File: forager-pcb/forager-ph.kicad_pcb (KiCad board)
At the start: 2 copper layers, 114.6 x 96.3 mm, 35 parts, among them J4 Conn_01x02_Pin

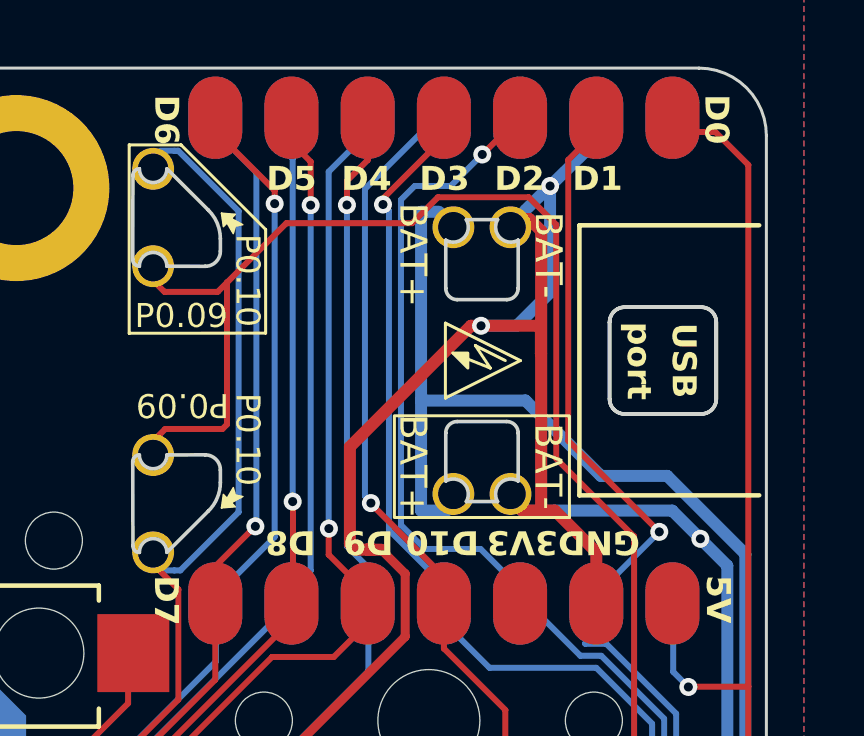
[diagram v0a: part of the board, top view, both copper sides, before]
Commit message: Re-inforce BAT+ connection with trace on both sides.
This may help if the copper is damaged while soldering, or when the
board is drilled during fabrication.
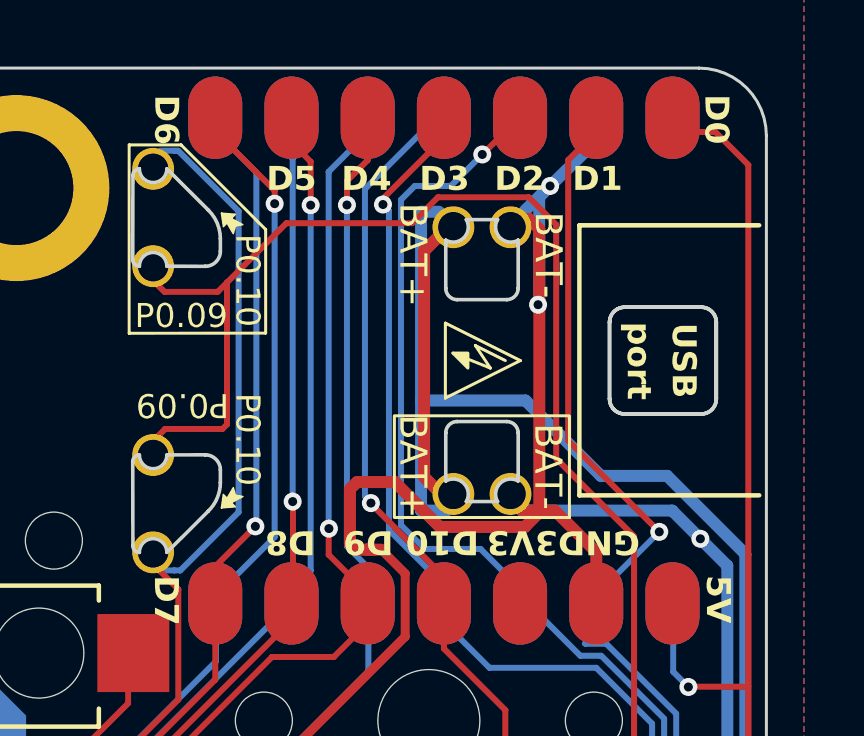
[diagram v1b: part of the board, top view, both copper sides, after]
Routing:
- net BAT: track 43.9 -> 52.9 mm
- net GND: track 204.8 -> 199.6 mm
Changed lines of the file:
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@@
 	)
 	(segment
-		(start 104.368 -37.128)
+		(start 104.561057 -33.697719)
 		(end 104.368 -33.890776)
 		(width 0.4)
@@
 	)
 	(segment
+		(start 110.639829 -41.862456)
+		(end 110.7135 -41.788785)
+		(width 0.4)
+		(layer "F.Cu")
+		(net 1)
+	)
+	(segment
 		(start 44.95 -19.83)
 		(end 44.95 -11.74)
@@
 	)
 	(segment
+		(start 110.68 -44.388023)
+		(end 110.353823 -44.7142)
+		(width 0.4)
+		(layer "F.Cu")
+		(net 1)
+	)
+	(segment
 		(start 101.575743 -0.325)
 		(end 105.19 -0.325)
@@
 	)
 	(segment
-		(start 108.74 -41.16)
-		(end 110.7135 -41.16)
+		(start 104.368 -35.71)
+		(end 104.609 -35.951)
 		(width 0.4)
 		(layer "F.Cu")
@@
 	)
 	(segment
-		(start 110.7335 -40.24)
-		(end 110.7435 -40.23)
+		(start 104.368 -33.890776)
+		(end 104.368 -35.71)
+		(width 0.4)
+		(layer "F.Cu")
+		(net 1)
+	)
+	(segment
+		(start 110.353823 -44.7142)
+		(end 110.109358 -44.7142)
 		(width 0.4)
 		(layer "F.Cu")
@@
 	)
 	(segment
-		(start 110.7135 -41.16)
-		(end 110.7335 -41.14)
-		(width 0.4)
-		(layer "F.Cu")
-		(net 1)
-	)
-	(segment
-		(start 110.7335 -41.14)
-		(end 110.7335 -40.24)
+		(start 110.199 -34.4555)
+		(end 110.68 -34.9365)
+		(width 0.4)
+		(layer "F.Cu")
+		(net 1)
+	)
+	(segment
+		(start 105.866072 -35.951)
+		(end 107.361572 -34.4555)
+		(width 0.4)
+		(layer "F.Cu")
+		(net 1)
+	)
+	(segment
+		(start 107.361572 -34.4555)
+		(end 110.199 -34.4555)
 		(width 0.4)
 		(layer "F.Cu")
@@
 	)
 	(segment
-		(start 110.7435 -44.324523)
-		(end 110.353823 -44.7142)
-		(width 0.4)
-		(layer "F.Cu")
-		(net 1)
-	)
-	(segment
-		(start 104.561057 -33.697719)
-		(end 104.94 -33.697719)
-		(width 0.4)
-		(layer "F.Cu")
-		(net 1)
-	)
-	(segment
-		(start 104.368 -33.890776)
-		(end 104.561057 -33.697719)
-		(width 0.4)
-		(layer "F.Cu")
-		(net 1)
-	)
-	(segment
 		(start 102.059603 -26.649)
 		(end 106.211 -30.800397)
@@
 	)
 	(segment
+		(start 110.68 -34.9365)
+		(end 110.68 -44.388023)
+		(width 0.4)
+		(layer "F.Cu")
+		(net 1)
+	)
+	(segment
 		(start 37.97 -4.76)
 		(end 35.9 -4.76)
@@
 	)
 	(segment
-		(start 110.7435 -35)
-		(end 110.7435 -44.324523)
-		(width 0.4)
-		(layer "F.Cu")
-		(net 1)
-	)
-	(segment
-		(start 108.74 -41.16)
-		(end 108.4 -41.16)
-		(width 0.4)
-		(layer "F.Cu")
-		(net 1)
-	)
-	(segment
 		(start 106.211 -30.800397)
 		(end 106.211 -32.898181)
@@
 	)
 	(segment
+		(start 104.609 -35.951)
+		(end 105.866072 -35.951)
+		(width 0.4)
+		(layer "F.Cu")
+		(net 1)
+	)
+	(segment
 		(start 100.017654 -26.801)
 		(end 100.169654 -26.649)
@@
 	)
 	(segment
-		(start 110.353823 -44.7142)
-		(end 110.109358 -44.7142)
+		(start 104.94 -33.697719)
+		(end 104.561057 -33.697719)
 		(width 0.4)
 		(layer "F.Cu")
@@
 	)
 	(segment
-		(start 108.4 -41.16)
-		(end 104.368 -37.128)
-		(width 0.4)
-		(layer "F.Cu")
-		(net 1)
-	)
-	(segment
 		(start 98.8 -26.122654)
 		(end 99.478346 -26.801)
@@
 	)
 	(via
-		(at 108.74 -41.16)
+		(at 110.639829 -41.862456)
 		(size 0.6)
 		(drill 0.3)
@@
 	)
 	(segment
+		(start 110.639829 -41.862456)
+		(end 110.677 -41.899627)
+		(width 0.4)
+		(layer "B.Cu")
+		(net 1)
+	)
+	(segment
 		(start 96.34 -20.87)
 		(end 81.41 -20.87)
@@
 	)
 	(segment
+		(start 110.677 -45.455808)
+		(end 111.040596 -45.819404)
+		(width 0.4)
+		(layer "B.Cu")
+		(net 1)
+	)
+	(segment
 		(start 112.58 -47.32)
 		(end 111.040596 -45.819404)
@@
 	)
 	(segment
-		(start 108.74 -41.16)
-		(end 109.93 -41.16)
-		(width 0.4)
-		(layer "B.Cu")
-		(net 1)
-	)
-	(segment
 		(start 105.19 -0.325)
 		(end 103.145 -0.325)
@@
 	)
 	(segment
-		(start 109.93 -41.16)
-		(end 111.040596 -42.270596)
-		(width 0.4)
-		(layer "B.Cu")
-		(net 1)
-	)
-	(segment
 		(start 116.948 -33.162)
 		(end 116.948 -23.698)
@@
 	)
 	(segment
-		(start 111.040596 -42.270596)
-		(end 111.040596 -45.819404)
+		(start 110.677 -41.899627)
+		(end 110.677 -45.455808)
 		(width 0.4)
 		(layer "B.Cu")
@@
 		(net 1)
 	)
-	(via
+	(segment
+		(start 106.84 -36.12)
+		(end 107.405 -35.555)
+		(width 0.4)
+		(layer "F.Cu")
+		(net 2)
+	)
+	(segment
+		(start 106.84 -43.65)
+		(end 106.84 -36.12)
+		(width 0.4)
+		(layer "F.Cu")
+		(net 2)
+	)
+	(segment
+		(start 107.318 -44.128)
+		(end 106.84 -43.65)
+		(width 0.4)
+		(layer "F.Cu")
+		(net 2)
+	)
+	(via

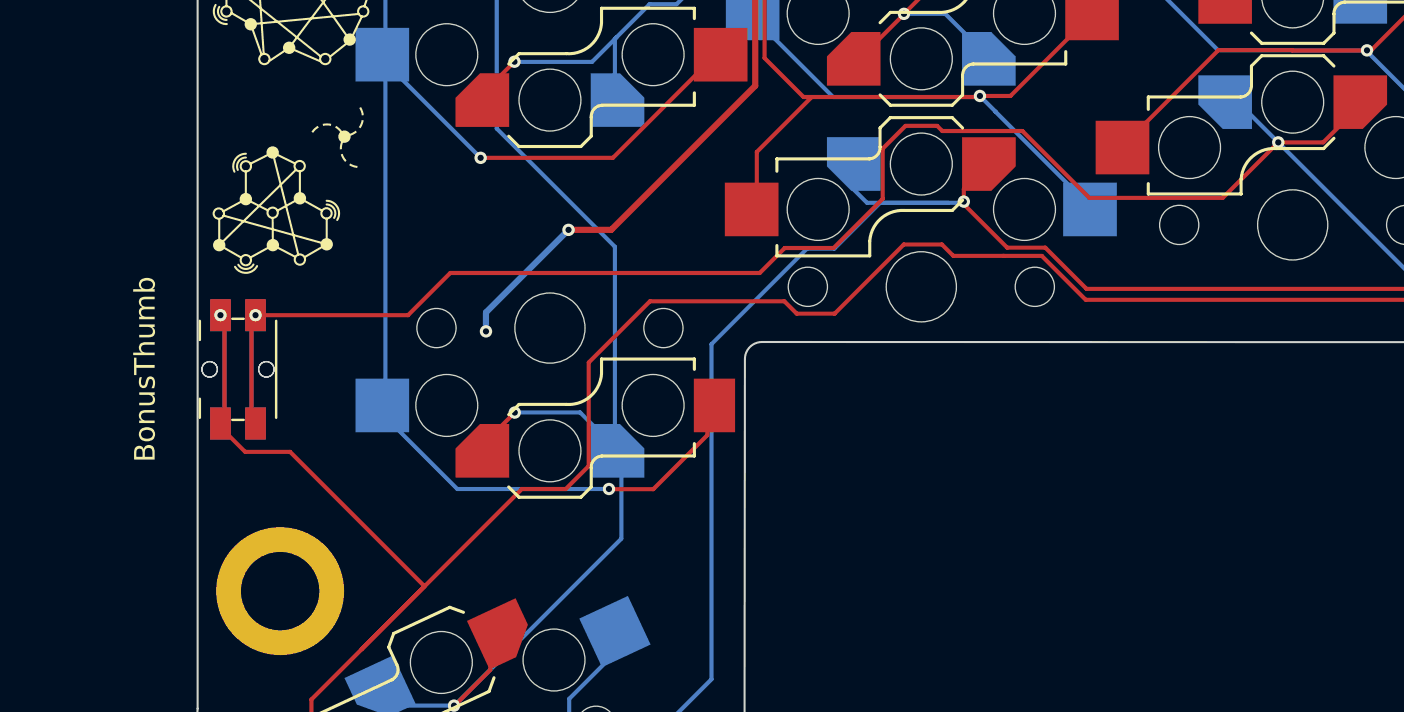
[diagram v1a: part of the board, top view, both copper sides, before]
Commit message: Bump Acid to v1.1.0, drop the unused 'bonus' thumb button
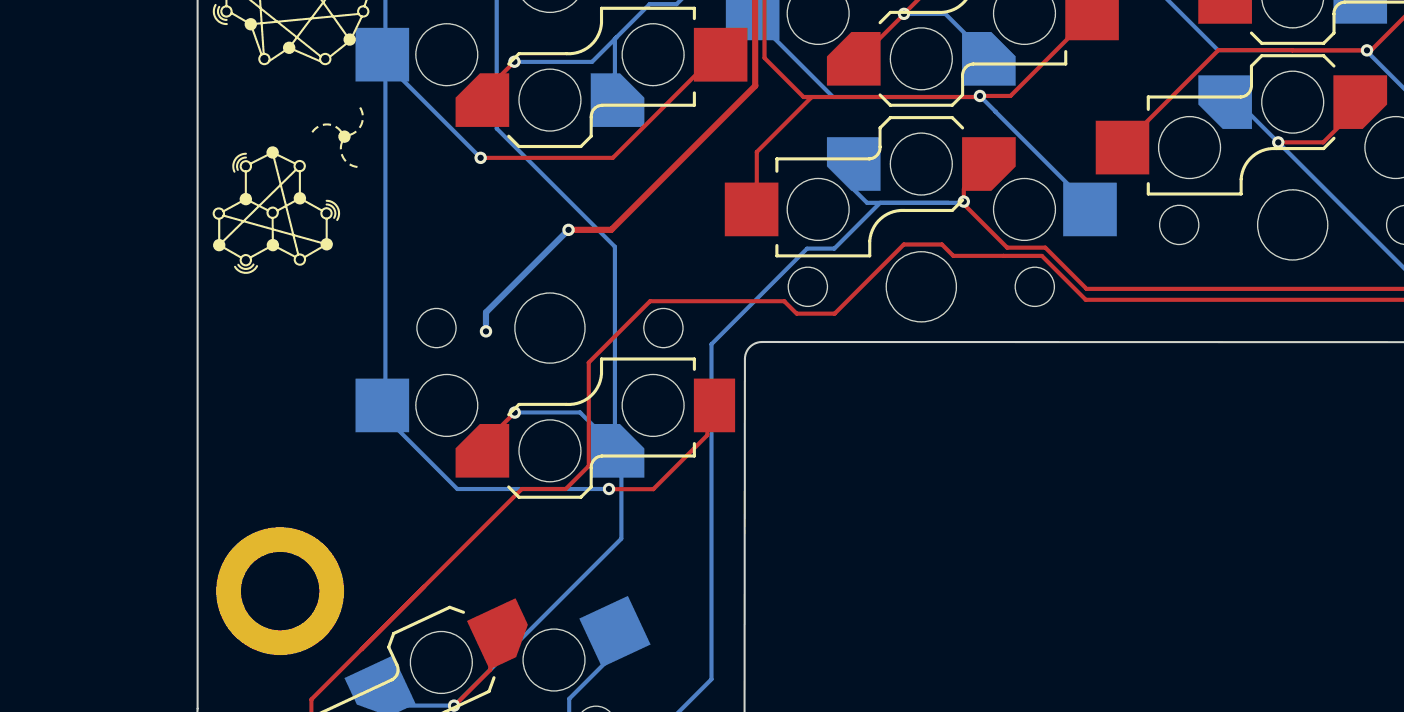
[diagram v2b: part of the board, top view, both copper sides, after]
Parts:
- removed BonusThumb (x2): Panasonic_EVQPUL_EVQPUC, Button_Switch_SMD:Panasonic_EVQPUL_EVQPUC
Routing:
- net R4: track 210.2 -> 143.2 mm, vias 4 -> 3
- net C5: track 215.7 -> 192.9 mm, vias 3 -> 2
